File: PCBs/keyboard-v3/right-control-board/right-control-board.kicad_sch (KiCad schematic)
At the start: 4 parts, among them IC101 USB2534-1080AEN, J101 USB4510-03-1-A, J102 USB4510-03-1-A, J103 GSB12J21C1EU

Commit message: Deleted delmes
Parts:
- removed IC101: USB2534-1080AEN, QFN50P600X600X100-37N-D, symbol USB-INTF:USB2534-1080AEN
- added U101: USB2534-1080AEN, QFN50P600X600X100-37N-D, symbol USB-INTF:USB2534-1080AEN
- added U102: STM32G0C1CEUx, Package_DFN_QFN:QFN-48-1EP_7x7mm_P0.5mm_EP5.6x5.6mm, symbol MCU_ST_STM32G0:STM32G0C1CEUx
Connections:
- new net: U102.49 (VSS), U102.7 (VSS)
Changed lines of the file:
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@@
+	)
+	(symbol
+		(lib_id "MCU_ST_STM32G0:STM32G0C1CEUx")
+		(at 114.3 109.22 0)
+		(unit 1)
+		(exclude_from_sim no)
+		(in_bom yes)
+		(on_board yes)
+		(dnp no)
+		(fields_autoplaced yes)
+		(property "Reference" "U102"
+			(at 116.4433 157.48 0)
+			(effects
+				(font
+					(size 1.27 1.27)
+				)
+				(justify left)
+			)
+		)
+		(property "Value" "STM32G0C1CEUx"
+			(at 116.4433 160.02 0)
+			(effects
+				(font
+					(size 1.27 1.27)
+				)
+				(justify left)
+			)
+		)
+		(property "Footprint" "Package_DFN_QFN:QFN-48-1EP_7x7mm_P0.5mm_EP5.6x5.6mm"
+			(at 88.9 154.94 0)
+			(effects
+				(font
+					(size 1.27 1.27)
+				)
+				(justify right)
+				(hide yes)
+			)
+		)
+		(property "Datasheet" "https://www.st.com/resource/en/datasheet/stm32g0c1ce.pdf"
+			(at 114.3 109.22 0)
+			(effects
+				(font
+					(size 1.27 1.27)
+				)
+				(hide yes)
+			)
+		)
+		(property "Description" "STMicroelectronics Arm Cortex-M0+ MCU, 512KB flash, 144KB RAM, 64 MHz, 1.7-3.6V, 44 GPIO, UFQFPN48"
+			(at 114.3 109.22 0)
+			(effects
+				(font
+					(size 1.27 1.27)
+				)
+				(hide yes)
+			)
+		)
+		(pin "3"
+		)
+		(pin "10"
+		)
+		(pin "28"
+		)
+		(pin "29"
+		)
+		(pin "38"
+		)
+		(pin "9"
+		)
+		(pin "5"
+		)
+		(pin "39"
+		)
+		(pin "31"
+		)
+		(pin "4"
+		)
+		(pin "49"
+		)
+		(pin "6"
+		)
+		(pin "30"
+		)
+		(pin "1"
+		)
+		(pin "2"
+		)
+		(pin "8"
+		)
+		(pin "7"
+		)
+		(pin "13"
+		)
+		(pin "40"
+		)
+		(pin "14"
+		)
+		(pin "15"
+		)
+		(pin "12"
+		)
+		(pin "16"
+		)
+		(pin "17"
+		)
+		(pin "41"
+		)
+		(pin "11"
+		)
+		(pin "18"
+		)
+		(pin "33"
+		)
+		(pin "43"
+		)
+		(pin "34"
+		)
+		(pin "25"
+		)
+		(pin "45"
+		)
+		(pin "35"
+		)
+		(pin "19"
+		)
+		(pin "36"
+		)
+		(pin "47"
+		)
+		(pin "37"
+		)
+		(pin "48"
+		)
+		(pin "22"
+		)
+		(pin "32"
+		)
+		(pin "20"
+		)
+		(pin "27"
+		)
+		(pin "23"
+		)
+		(pin "21"
+		)
+		(pin "42"
+		)
+		(pin "44"
+		)
+		(pin "46"
+		)
+		(pin "24"
+		)
+		(pin "26"
+		)
+		(instances
+			(project ""
+				(path "/982f1c46-f6d6-42a2-bf2a-9fb0e913f11f"
+					(reference "U102")
+					(unit 1)
+				)
+			)
+		)
 	)
 	(symbol
@@
 	(symbol
 		(lib_id "USB-INTF:USB2534-1080AEN")
-		(at 139.7 93.98 0)
+		(at 195.58 45.72 0)
 		(unit 1)
 		(exclude_from_sim no)
@@
 		(dnp no)
 		(fields_autoplaced yes)
-		(property "Reference" "IC101"
-			(at 224.79 87.5598 0)
+		(property "Reference" "U101"
+			(at 195.58 40.64 0)
 			(effects
 				(font
@@
 		)
 		(property "Value" "USB2534-1080AEN"
-			(at 224.79 90.0998 0)
+			(at 195.58 43.18 0)
 			(effects
 				(font
@@
 		)
 		(property "Footprint" "QFN50P600X600X100-37N-D"
-			(at 214.63 150.8 0)
-			(effects
-				(font
-					(size 1.27 1.27)
-				)
-				(justify left top)
+			(at 195.58 134.62 0)
+			(effects
+				(font
+					(size 1.27 1.27)
+				)
 				(hide yes)
 			)
 		)
 		(property "Datasheet" "https://www.arrow.com/en/products/usb2534-1080aen/microchip-technology?region=nac"
-			(at 214.63 250.8 0)
-			(effects
-				(font
-					(size 1.27 1.27)
-				)
-				(justify left top)
+			(at 195.58 139.7 0)
+			(effects
+				(font
+					(size 1.27 1.27)
+				)
 				(hide yes)
 			)
 		)
 		(property "Description" "Microchip USB2534-1080AEN, USB Controller, USB 2.0, 3.3 V, 36-Pin SQFN"
-			(at 139.7 93.98 0)
+			(at 195.58 137.16 0)
 			(effects
 				(font
@@
 		)
 		(property "Height" "1"
-			(at 214.63 450.8 0)
-			(effects
-				(font
-					(size 1.27 1.27)
-				)
-				(justify left top)
-				(hide yes)
-			)
-		)
-		(property "Mouser Part Number" "579-USB2534-1080AEN"
-			(at 214.63 550.8 0)
-			(effects
-				(font
-					(size 1.27 1.27)
-				)
-				(justify left top)
-				(hide yes)
-			)
-		)
-		(property "Mouser Price/Stock" "https://www.mouser.co.uk/ProductDetail/Microchip-Technology/USB2534-1080AEN?qs=3i1%252BhB2xfwlmD2gKDIPkSA%3D%3D"
-			(at 214.63 650.8 0)
-			(effects
-				(font
-					(size 1.27 1.27)
-				)
-				(justify left top)
-				(hide yes)
-			)
-		)
-		(property "Manufacturer_Name" "Microchip"
-			(at 214.63 750.8 0)
-			(effects
-				(font
-					(size 1.27 1.27)
-				)
-				(justify left top)
-				(hide yes)
-			)
-		)
-		(property "Manufacturer_Part_Number" "USB2534-1080AEN"
-			(at 214.63 850.8 0)
-			(effects
-				(font
-					(size 1.27 1.27)
-				)
-				(justify left top)
-				(hide yes)
-			)
+			(at 195.58 142.24 0)
+			(effects
+				(font
+					(size 1.27 1.27)
+				)
+				(hide yes)
+			)
+		)
+		(pin "3"
+		)
+		(pin "26"
+		)
+		(pin "30"
+		)
+		(pin "31"
+		)
+		(pin "1"
 		)
 		(pin "2"
 		)
+		(pin "7"
+		)
+		(pin "24"
+		)
+		(pin "8"
+		)
+		(pin "12"
+		)
+		(pin "16"
+		)
+		(pin "18"
+		)
+		(pin "20"
+		)
+		(pin "27"
+		)
+		(pin "4"
+		)
+		(pin "9"
+		)
+		(pin "22"
+		)
+		(pin "6"
+		)
+		(pin "28"
+		)
+		(pin "25"
+		)
+		(pin "34"
+		)
+		(pin "37"
+		)
+		(pin "11"
+		)
+		(pin "15"
+		)
+		(pin "17"
+		)
+		(pin "33"
+		)
+		(pin "19"
+		)
+		(pin "29"
+		)
+		(pin "21"
+		)
+		(pin "10"
+		)
+		(pin "23"
+		)
+		(pin "14"
+		)
+		(pin "32"
+		)
+		(pin "36"
+		)
+		(pin "13"
+		)
 		(pin "35"
 		)
-		(pin "11"
-		)
-		(pin "4"
-		)
-		(pin "6"
-		)
-		(pin "37"
-		)
-		(pin "25"
-		)
 		(pin "5"
-		)
-		(pin "14"
-		)
-		(pin "3"
-		)
-		(pin "29"
-		)
-		(pin "36"
-		)
-		(pin "33"
-		)
-		(pin "28"
-		)
-		(pin "27"
-		)
-		(pin "15"
-		)
-		(pin "1"
-		)
-		(pin "10"
-		)
-		(pin "13"
-		)
-		(pin "12"
-		)
-		(pin "9"
-		)
-		(pin "26"
-		)
-		(pin "8"
-		)
-		(pin "17"
-		)
-		(pin "7"
-		)
-		(pin "32"
-		)
-		(pin "31"
-		)
-		(pin "30"
-		)
-		(pin "16"
-		)
-		(pin "34"
-		)
-		(pin "18"
-		)
-		(pin "20"
-		)
-		(pin "24"
-		)
-		(pin "19"
-		)
-		(pin "23"
-		)
-		(pin "21"
-		)
-		(pin "22"
 		)
 		(instances
 			(project ""
 				(path "/982f1c46-f6d6-42a2-bf2a-9fb0e913f11f"
-					(reference "IC101")
+					(reference "U101")
 					(unit 1)
 				)

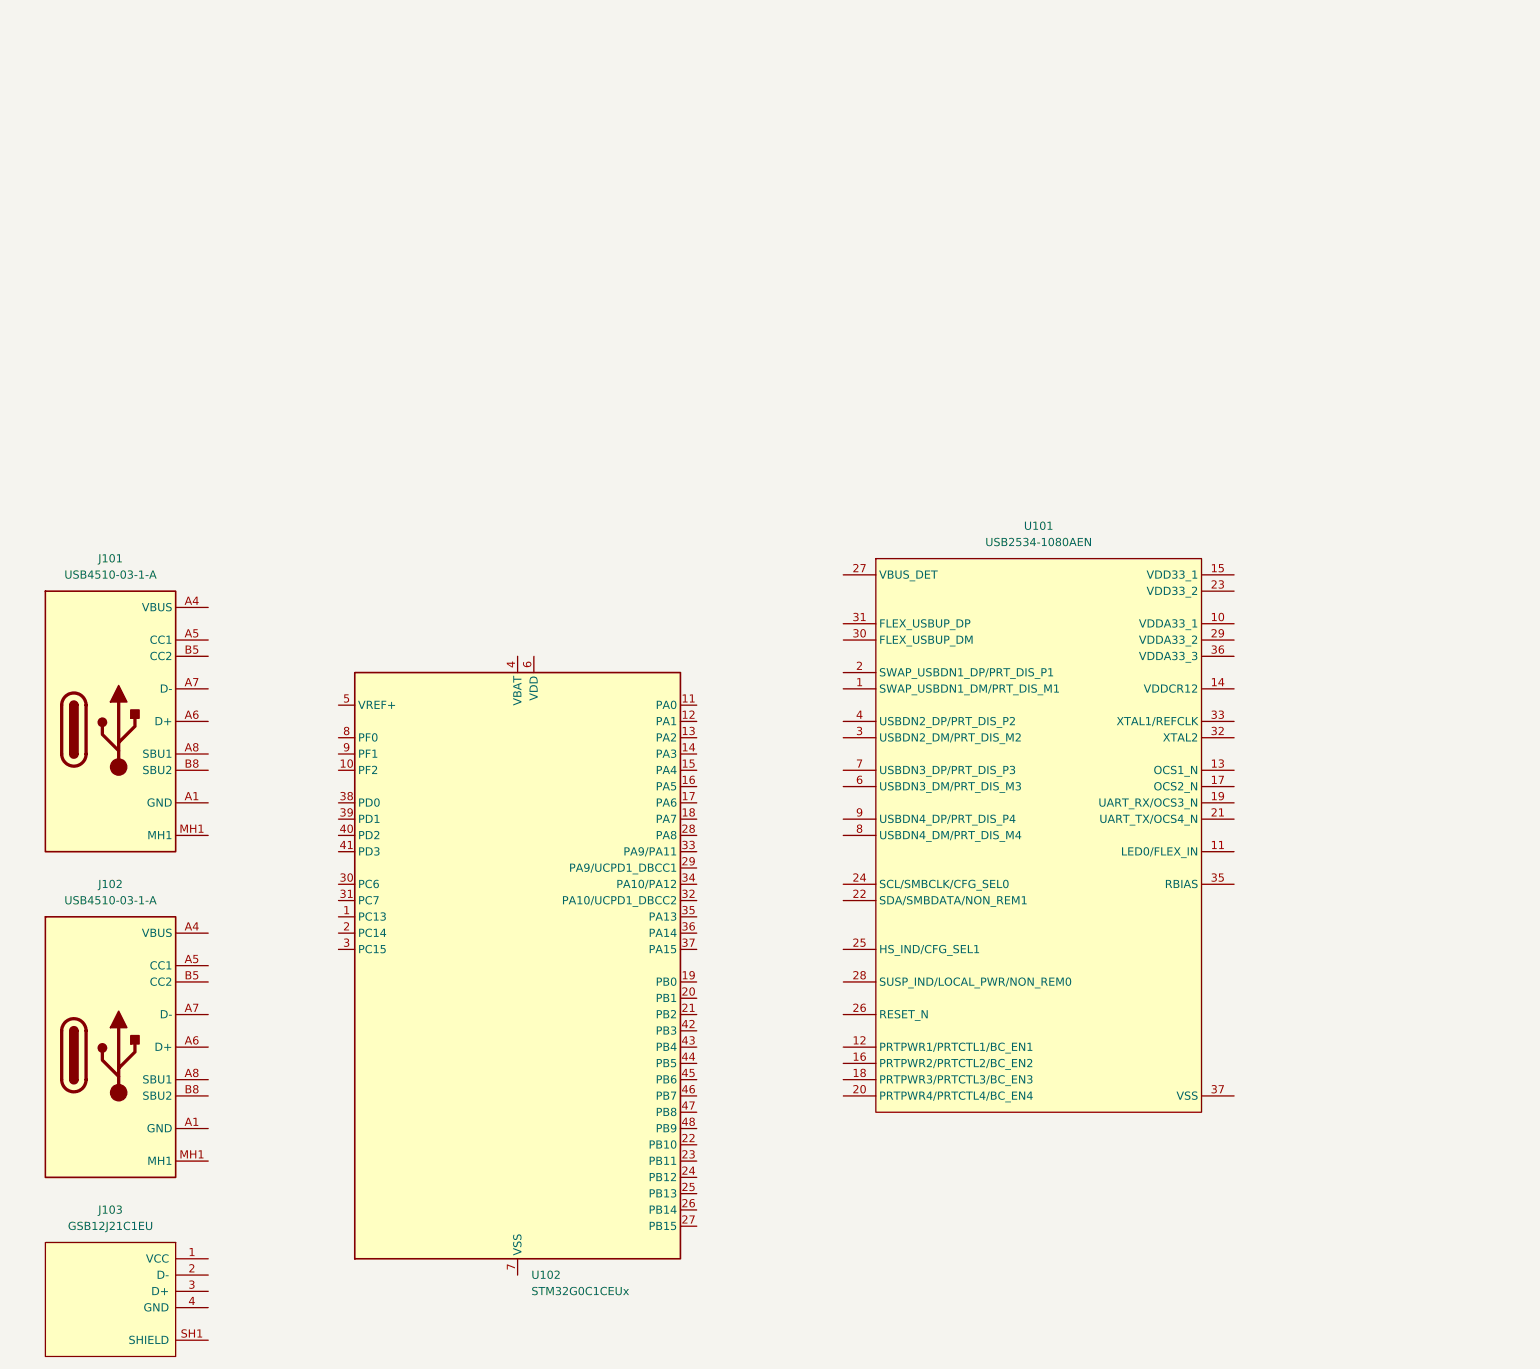
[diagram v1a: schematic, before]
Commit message: Updated right-control-board layout
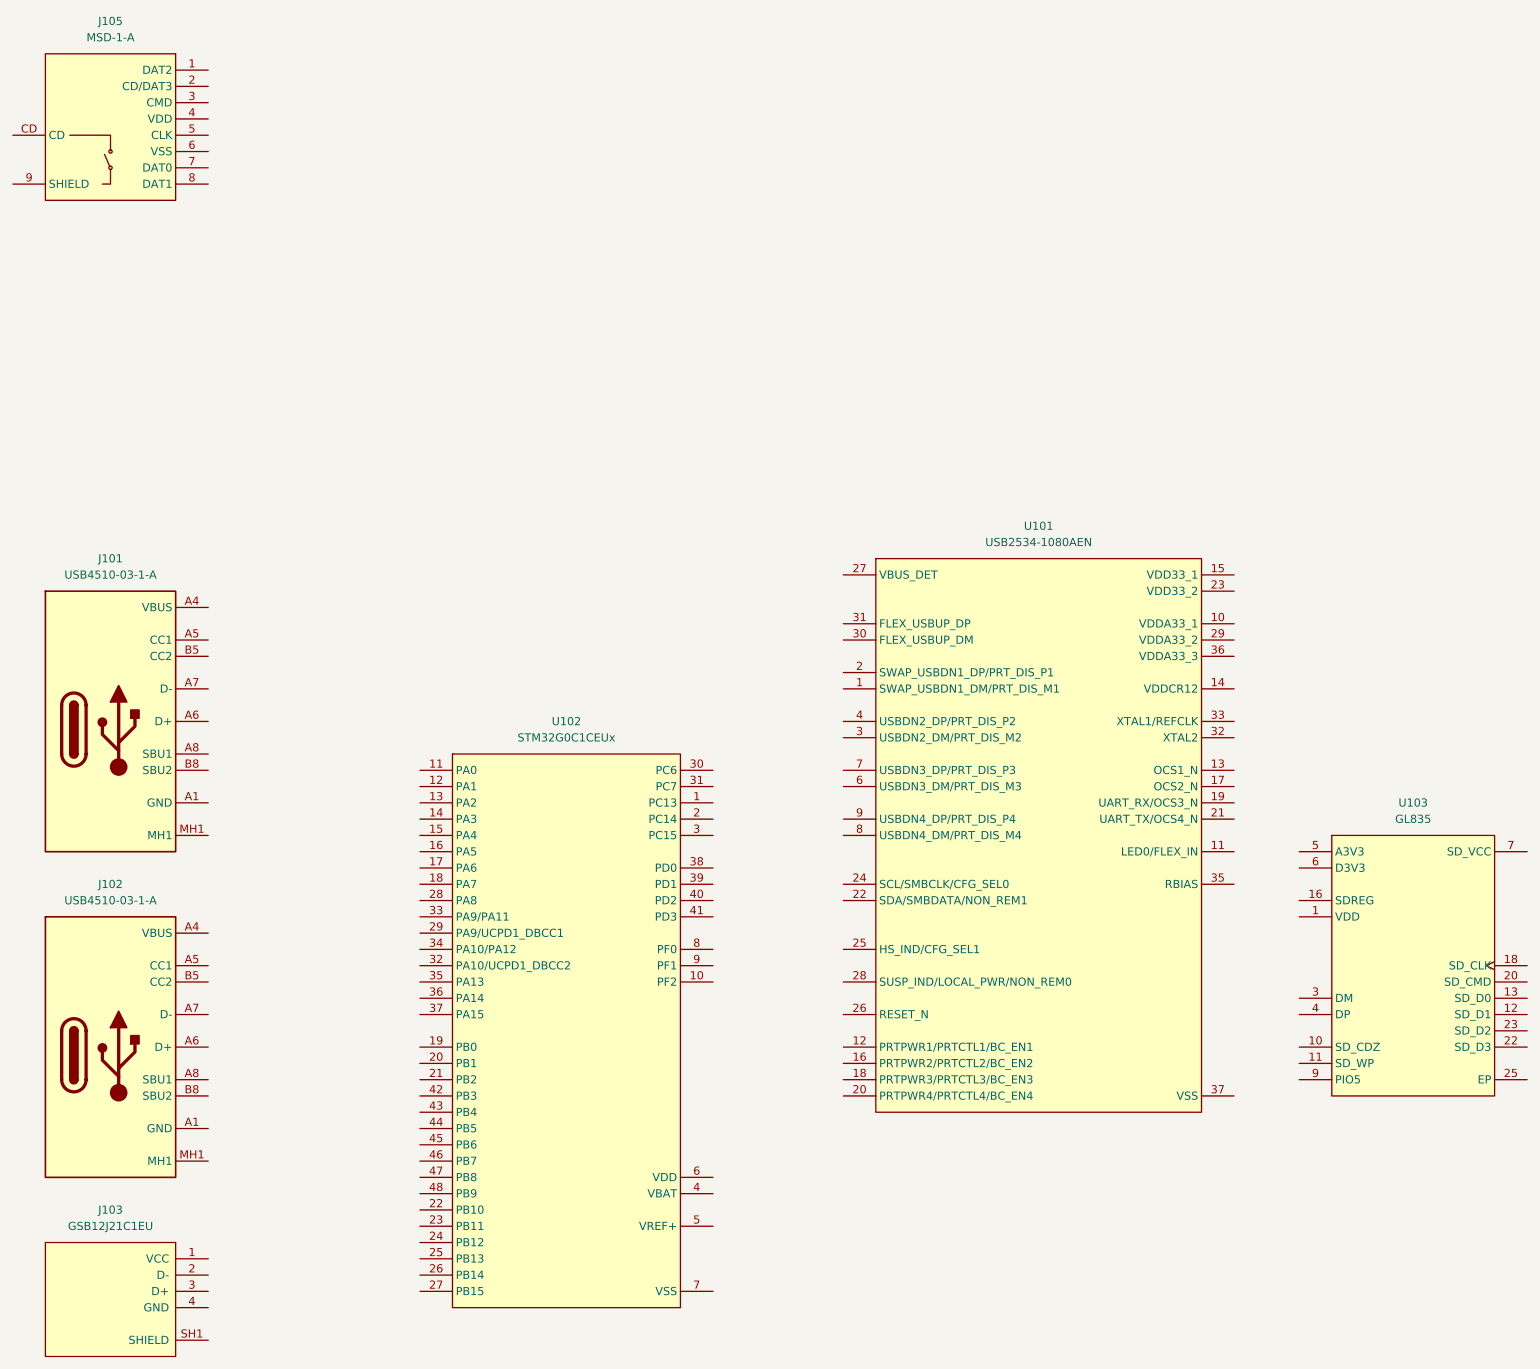
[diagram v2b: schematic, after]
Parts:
- removed U102: STM32G0C1CEUx, Package_DFN_QFN:QFN-48-1EP_7x7mm_P0.5mm_EP5.6x5.6mm, symbol MCU_ST_STM32G0:STM32G0C1CEUx
- added J105: MSD-1-A, project_footprints:MSD1A, symbol SD-CONN:MSD-1-A
- added U102: STM32G0C1CEUx, project_footprints:QFN50P700X700X60-49N-D, symbol STM32:STM32G0C1CEUx
- added U103: GL835, project_footprints:QFN50P400X400X100-25N-D, symbol USB-INTF:GL835
- J101, J102: footprint keyboard_footprints:USB4510031A -> project_footprints:USB4510031A
- J103: footprint keyboard_footprints:AMPHENOL_GSB12J21C1EU -> project_footprints:GSB12J21C1EU
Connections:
- new net: U103.14 (NC), U103.15 (NC), U103.17 (NC), U103.19 (NC), U103.2 (NC), U103.21 (NC), U103.24 (NC), U103.8 (NC)
- new net: J105.10 (SHIELD), J105.11 (SHIELD), J105.12 (SHIELD), J105.9 (SHIELD)
- new net: U102.49 (VSS), U102.7 (VSS)

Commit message: Right control board schematic almost done
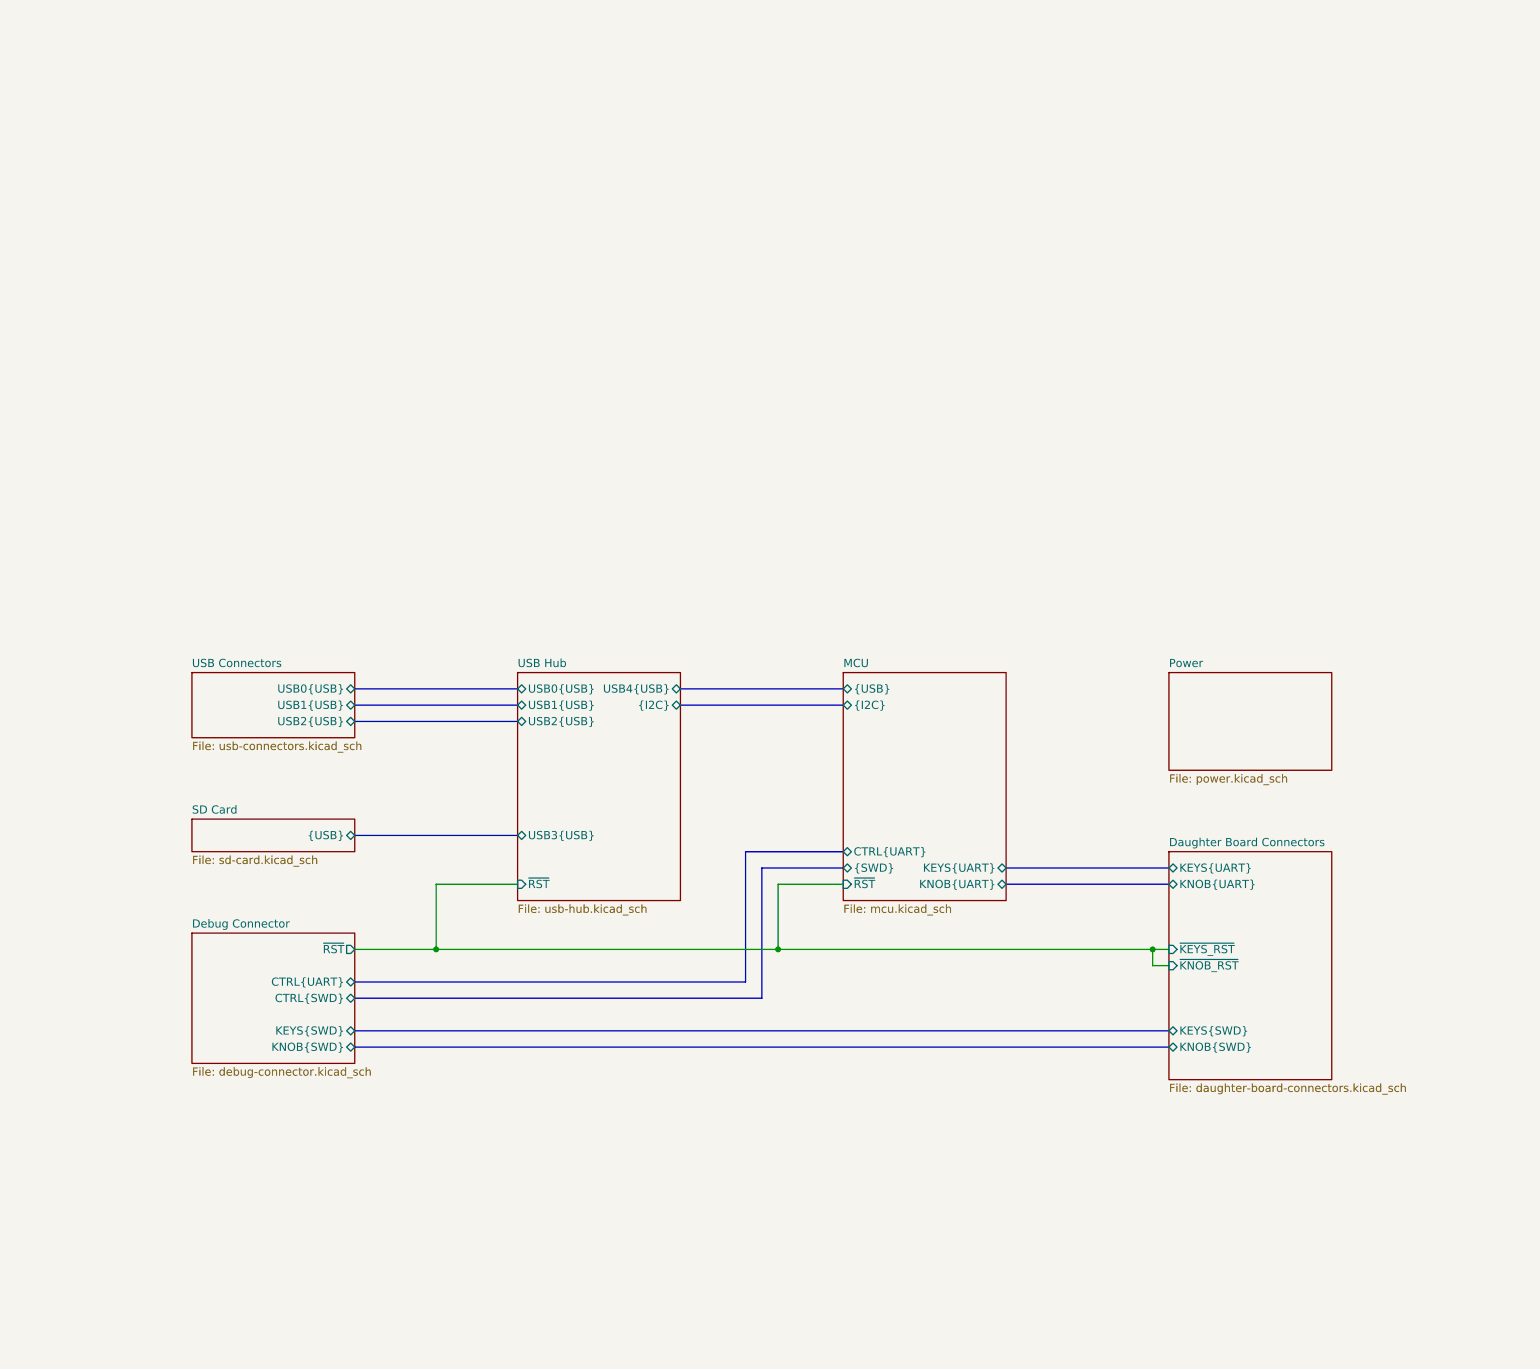
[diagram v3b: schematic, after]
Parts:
- removed J101, J102: USB4510-03-1-A, project_footprints:USB4510031A, symbol USB-CONN:USB4510-03-1-A
- removed J103: GSB12J21C1EU, project_footprints:GSB12J21C1EU, symbol USB-CONN:GSB12J21C1EU
- removed J105: MSD-1-A, project_footprints:MSD1A, symbol SD-CONN:MSD-1-A
- removed U101: USB2534-1080AEN, QFN50P600X600X100-37N-D, symbol USB-INTF:USB2534-1080AEN
- removed U102: STM32G0C1CEUx, project_footprints:QFN50P700X700X60-49N-D, symbol STM32:STM32G0C1CEUx
- removed U103: GL835, project_footprints:QFN50P400X400X100-25N-D, symbol USB-INTF:GL835
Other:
- added sheet Daughter Board Connectors (daughter-board-connectors.kicad_sch)
- added sheet Debug Connector (debug-connector.kicad_sch)
- added sheet MCU (mcu.kicad_sch)
- added sheet Power (power.kicad_sch)
- added sheet SD Card (sd-card.kicad_sch)
- added sheet USB Connectors (usb-connectors.kicad_sch)
- added sheet USB Hub (usb-hub.kicad_sch)
